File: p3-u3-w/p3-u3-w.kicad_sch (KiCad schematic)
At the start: 0 parts

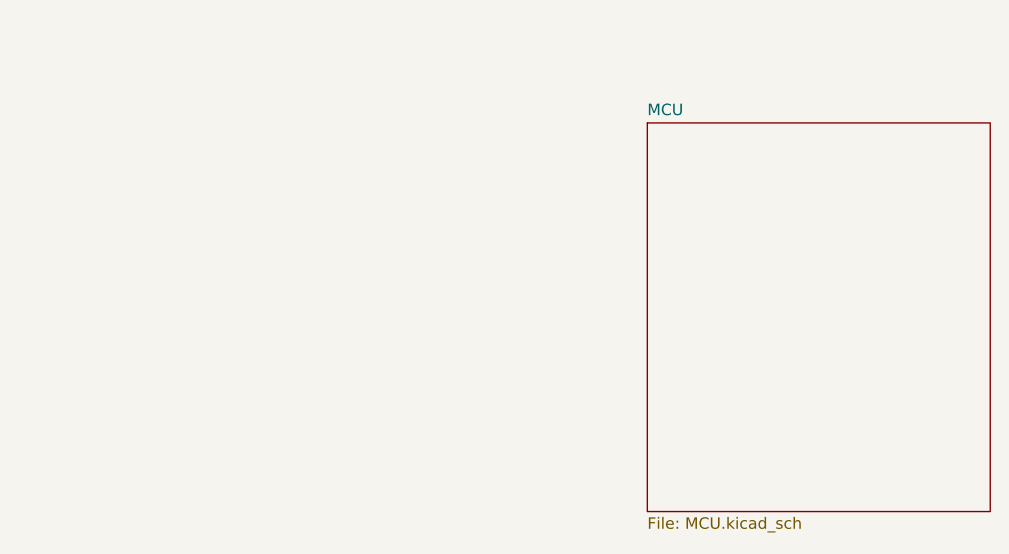
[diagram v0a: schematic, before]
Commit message: added in i2C pullups, added in display
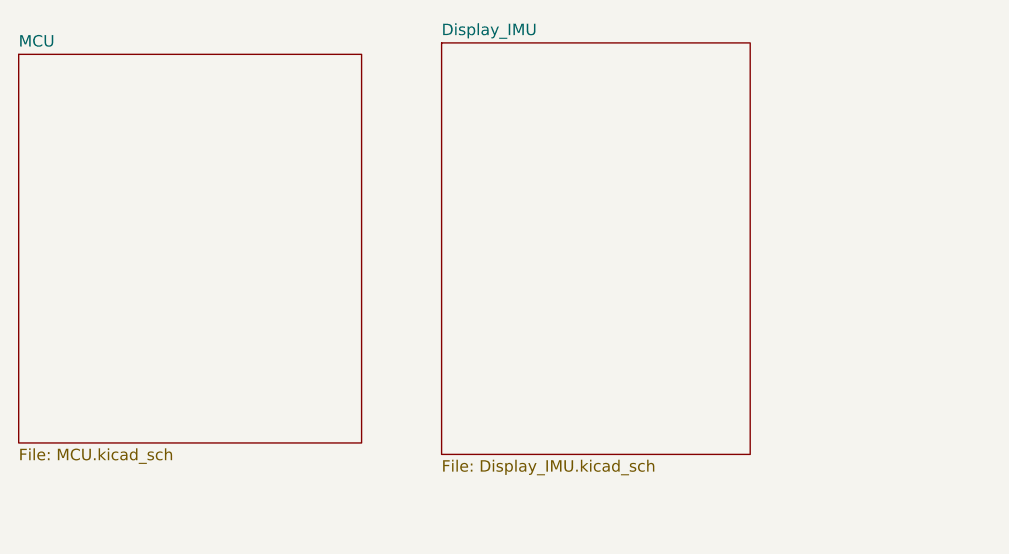
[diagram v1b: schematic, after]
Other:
- added sheet Display_IMU (Display_IMU.kicad_sch)
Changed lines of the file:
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@@
 	(paper "A4")
 	(sheet
-		(at 123.19 50.8)
+		(at 53.34 43.18)
 		(size 38.1 43.18)
 		(exclude_from_sim no)
@@
 		)
 		(property "Sheetname" "MCU"
-			(at 123.19 50.0884 0)
+			(at 53.34 42.4684 0)
 			(effects
 				(font
@@
 		)
 		(property "Sheetfile" "MCU.kicad_sch"
-			(at 123.19 94.5646 0)
+			(at 53.34 86.9446 0)
 			(effects
 				(font
@@
 				)
 			)
+		)
+	)
+	(sheet
+		(at 100.33 41.91)
+		(size 34.29 45.72)
+		(exclude_from_sim no)
+		(in_bom yes)
+		(on_board yes)
+		(dnp no)
+		(fields_autoplaced yes)
+		(stroke
+			(width 0.1524)
+			(type solid)
+		)
+		(fill
+			(color 0 0 0 0.0000)
+		)
+		(property "Sheetname" "Display_IMU"
+			(at 100.33 41.1984 0)
+			(effects
+				(font
+					(size 1.27 1.27)
+				)
+				(justify left bottom)
+			)
+		)
+		(property "Sheetfile" "Display_IMU.kicad_sch"
+			(at 100.33 88.2146 0)
+			(effects
+				(font
+					(size 1.27 1.27)
+				)
+				(justify left top)
+			)
+		)
+		(instances
+			(project "p3-u3-w"
+				(path "/afed05dd-3bce-4903-b4b6-a2a13f579b42"
+					(page "3")
+				)
+			)

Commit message: added in power side and mostly finished schematics :)
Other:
- added sheet SD_DAC (SD_DAC.kicad_sch)
- added sheet USB_PWR (USB_PWR.kicad_sch)
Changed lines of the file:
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@@
 	(paper "A4")
 	(sheet
-		(at 53.34 43.18)
+		(at 99.06 38.1)
 		(size 38.1 43.18)
 		(exclude_from_sim no)
@@
 		)
 		(property "Sheetname" "MCU"
-			(at 53.34 42.4684 0)
+			(at 99.06 37.3884 0)
 			(effects
 				(font
@@
 		)
 		(property "Sheetfile" "MCU.kicad_sch"
-			(at 53.34 86.9446 0)
+			(at 99.06 81.8646 0)
 			(effects
 				(font
@@
 	)
 	(sheet
-		(at 100.33 41.91)
+		(at 158.75 38.1)
+		(size 36.83 48.26)
+		(exclude_from_sim no)
+		(in_bom yes)
+		(on_board yes)
+		(dnp no)
+		(fields_autoplaced yes)
+		(stroke
+			(width 0.1524)
+			(type solid)
+		)
+		(fill
+			(color 0 0 0 0.0000)
+		)
+		(property "Sheetname" "SD_DAC"
+			(at 158.75 37.3884 0)
+			(effects
+				(font
+					(size 1.27 1.27)
+				)
+				(justify left bottom)
+			)
+		)
+		(property "Sheetfile" "SD_DAC.kicad_sch"
+			(at 158.75 86.9446 0)
+			(effects
+				(font
+					(size 1.27 1.27)
+				)
+				(justify left top)
+			)
+		)
+		(instances
+			(project "p3-u3-w"
+				(path "/afed05dd-3bce-4903-b4b6-a2a13f579b42"
+					(page "4")
+				)
+			)
+		)
+	)
+	(sheet
+		(at 38.1 38.1)
 		(size 34.29 45.72)
 		(exclude_from_sim no)
@@
 		)
 		(property "Sheetname" "Display_IMU"
-			(at 100.33 41.1984 0)
+			(at 38.1 37.3884 0)
 			(effects
 				(font
@@
 		)
 		(property "Sheetfile" "Display_IMU.kicad_sch"
-			(at 100.33 88.2146 0)
+			(at 38.1 84.4046 0)
 			(effects
 				(font
@@
 				)
 			)
+		)
+	)
+	(sheet
+		(at 99.06 99.06)
+		(size 40.64 52.07)
+		(exclude_from_sim no)
+		(in_bom yes)
+		(on_board yes)
+		(dnp no)
+		(fields_autoplaced yes)
+		(stroke
+			(width 0.1524)
+			(type solid)
+		)
+		(fill
+			(color 0 0 0 0.0000)
+		)
+		(property "Sheetname" "USB_PWR"
+			(at 99.06 98.3484 0)
+			(effects
+				(font
+					(size 1.27 1.27)
+				)
+				(justify left bottom)
+			)
+		)
+		(property "Sheetfile" "USB_PWR.kicad_sch"
+			(at 99.06 151.7146 0)
+			(effects
+				(font
+					(size 1.27 1.27)
+				)
+				(justify left top)
+			)
+		)
+		(instances
+			(project "p3-u3-w"
+				(path "/afed05dd-3bce-4903-b4b6-a2a13f579b42"
+					(page "5")
+				)
+			)
